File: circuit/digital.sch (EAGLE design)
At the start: 28 parts, among them IC1 MCP1701-5V, IC2 MCP1700-3.3V, X1 MINI-USB-SCHIELD-32005-301

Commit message: - вывели 4 IO пина на всяк случай, для LCD
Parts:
- added X10, X9: (no value), con-phoenix-254:MPT4
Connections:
- new net N$10: U$1G$9.PD5, X10-4.1
- new net N$6: U$1G$9.PD2, X10-1.1
- new net N$8: U$1G$9.PD3, X10-2.1
- new net N$9: U$1G$9.PD4, X10-3.1
- new net SWCLK: U$1G$2.PA14, X9-3.1
- new net SWDIO: U$1G$2.PA13, X9-2.1
- net +3V3: now also X9-1.1
- net GND: now also X9-4.1
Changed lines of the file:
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@@
 <part name="C10" library="rcl" deviceset="C-EU" device="C0603" value="1mk"/>
 <part name="P+2" library="supply1" deviceset="+5V" device=""/>
+<part name="X9" library="con-phoenix-254" deviceset="MPT4" device=""/>
+<part name="+3V4" library="supply1" deviceset="+3V3" device=""/>
+<part name="GND12" library="supply1" deviceset="GND" device=""/>
+<part name="X10" library="con-phoenix-254" deviceset="MPT4" device=""/>
 </parts>
 <sheets>
@@
 <instance part="C10" gate="G$1" x="25.4" y="93.98"/>
 <instance part="P+2" gate="1" x="25.4" y="104.14"/>
+<instance part="X9" gate="-1" x="177.8" y="5.08"/>
+<instance part="X9" gate="-2" x="177.8" y="0"/>
+<instance part="X9" gate="-3" x="177.8" y="-5.08"/>
+<instance part="X9" gate="-4" x="177.8" y="-10.16"/>
+<instance part="+3V4" gate="G$1" x="170.18" y="10.16"/>
+<instance part="GND12" gate="1" x="170.18" y="-15.24"/>
+<instance part="X10" gate="-1" x="127" y="-48.26"/>
+<instance part="X10" gate="-2" x="127" y="-53.34"/>
+<instance part="X10" gate="-3" x="127" y="-58.42"/>
+<instance part="X10" gate="-4" x="127" y="-63.5"/>
 </instances>
 <busses>
@@
 <junction x="12.7" y="88.9"/>
 <junction x="-2.54" y="88.9"/>
+</segment>
+<segment>
+<pinref part="GND12" gate="1" pin="GND"/>
+<wire x1="170.18" y1="-12.7" x2="170.18" y2="-10.16" width="0.1524" layer="91"/>
+<pinref part="X9" gate="-4" pin="1"/>
+<wire x1="170.18" y1="-10.16" x2="175.26" y2="-10.16" width="0.1524" layer="91"/>
 </segment>
 </net>
@@
 <junction x="0" y="40.64"/>
 </segment>
+<segment>
+<pinref part="X9" gate="-1" pin="1"/>
+<pinref part="+3V4" gate="G$1" pin="+3V3"/>
+<wire x1="175.26" y1="5.08" x2="170.18" y2="5.08" width="0.1524" layer="91"/>
+<wire x1="170.18" y1="5.08" x2="170.18" y2="7.62" width="0.1524" layer="91"/>
+</segment>
 </net>
 <net name="V+" class="0">
@@
 </segment>
 </net>
+<net name="SWDIO" class="0">
+<segment>
+<pinref part="U$1" gate="G$2" pin="PA13"/>
+<wire x1="50.8" y1="15.24" x2="40.64" y2="15.24" width="0.1524" layer="91"/>
+<label x="40.64" y="15.494" size="1.778" layer="95"/>
+</segment>
+<segment>
+<pinref part="X9" gate="-2" pin="1"/>
+<wire x1="175.26" y1="0" x2="162.56" y2="0" width="0.1524" layer="91"/>
+<label x="162.814" y="0.508" size="1.778" layer="95"/>
+</segment>
+</net>
+<net name="SWCLK" class="0">
+<segment>
+<pinref part="U$1" gate="G$2" pin="PA14"/>
+<wire x1="50.8" y1="12.7" x2="40.64" y2="12.7" width="0.1524" layer="91"/>
+<label x="40.386" y="12.954" size="1.778" layer="95"/>
+</segment>
+<segment>
+<pinref part="X9" gate="-3" pin="1"/>
+<wire x1="175.26" y1="-5.08" x2="162.56" y2="-5.08" width="0.1524" layer="91"/>
+<label x="162.814" y="-4.572" size="1.778" layer="95"/>
+</segment>
+</net>
+<net name="N$6" class="0">
+<segment>
+<pinref part="U$1" gate="G$9" pin="PD2"/>
+<wire x1="86.36" y1="-53.34" x2="114.3" y2="-53.34" width="0.1524" layer="91"/>
+<wire x1="114.3" y1="-53.34" x2="114.3" y2="-48.26" width="0.1524" layer="91"/>
+<pinref part="X10" gate="-1" pin="1"/>
+<wire x1="114.3" y1="-48.26" x2="124.46" y2="-48.26" width="0.1524" layer="91"/>
+</segment>
+</net>
+<net name="N$8" class="0">
+<segment>
+<pinref part="U$1" gate="G$9" pin="PD3"/>
+<wire x1="86.36" y1="-55.88" x2="119.38" y2="-55.88" width="0.1524" layer="91"/>
+<wire x1="119.38" y1="-55.88" x2="119.38" y2="-53.34" width="0.1524" layer="91"/>
+<pinref part="X10" gate="-2" pin="1"/>
+<wire x1="119.38" y1="-53.34" x2="124.46" y2="-53.34" width="0.1524" layer="91"/>
+</segment>
+</net>
+<net name="N$9" class="0">
+<segment>
+<pinref part="U$1" gate="G$9" pin="PD4"/>
+<pinref part="X10" gate="-3" pin="1"/>
+<wire x1="86.36" y1="-58.42" x2="124.46" y2="-58.42" width="0.1524" layer="91"/>
+</segment>
+</net>
+<net name="N$10" class="0">
+<segment>
+<pinref part="U$1" gate="G$9" pin="PD5"/>
+<wire x1="86.36" y1="-60.96" x2="121.92" y2="-60.96" width="0.1524" layer="91"/>
+<wire x1="121.92" y1="-60.96" x2="121.92" y2="-63.5" width="0.1524" layer="91"/>
+<pinref part="X10" gate="-4" pin="1"/>
+<wire x1="121.92" y1="-63.5" x2="124.46" y2="-63.5" width="0.1524" layer="91"/>
+</segment>
+</net>

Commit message: - подтяжка по USB
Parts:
- added R4: 1.5k, rcl:R-EU_R0603
- L2: value MMZ1608B102C -> 100mk
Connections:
- net +3V3: now also R4.1
- net GND: now also U$1G$11.VBAT
- net N$2: now also R4.2
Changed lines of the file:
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@@
 </classes>
 <parts>
-<part name="L2" library="rcl" deviceset="L-US" device="0204/7" value="MMZ1608B102C"/>
+<part name="L2" library="rcl" deviceset="L-US" device="0204/7" value="100mk"/>
 <part name="C11" library="rcl" deviceset="C-EU" device="C0603" value="100n"/>
 <part name="C12" library="rcl" deviceset="C-EU" device="C0805" value="10mk"/>
@@
 <part name="GND12" library="supply1" deviceset="GND" device=""/>
 <part name="X10" library="con-phoenix-254" deviceset="MPT4" device=""/>
+<part name="R4" library="rcl" deviceset="R-EU_" device="R0603" value="1.5k"/>
+<part name="+3V5" library="supply1" deviceset="+3V3" device=""/>
 </parts>
 <sheets>
@@
 <instance part="X10" gate="-3" x="127" y="-58.42"/>
 <instance part="X10" gate="-4" x="127" y="-63.5"/>
+<instance part="R4" gate="G$1" x="45.72" y="48.26" rot="R90"/>
+<instance part="+3V5" gate="G$1" x="40.64" y="45.72"/>
 </instances>
 <busses>
@@
 <pinref part="X1" gate="G$1" pin="3"/>
 <pinref part="R2" gate="G$1" pin="2"/>
-<wire x1="53.34" y1="53.34" x2="43.18" y2="53.34" width="0.1524" layer="91"/>
+<wire x1="53.34" y1="53.34" x2="45.72" y2="53.34" width="0.1524" layer="91"/>
+<wire x1="45.72" y1="53.34" x2="43.18" y2="53.34" width="0.1524" layer="91"/>
 <wire x1="43.18" y1="53.34" x2="43.18" y2="50.8" width="0.1524" layer="91"/>
+<pinref part="R4" gate="G$1" pin="2"/>
+<junction x="45.72" y="53.34"/>
 </segment>
 </net>
@@
 <junction x="-7.62" y="25.4"/>
 <junction x="-7.62" y="33.02"/>
+<pinref part="U$1" gate="G$11" pin="VBAT"/>
+<wire x1="12.7" y1="2.54" x2="12.7" y2="7.62" width="0.1524" layer="91"/>
 </segment>
 <segment>
@@
 <wire x1="170.18" y1="5.08" x2="170.18" y2="7.62" width="0.1524" layer="91"/>
 </segment>
-</net>
+<segment>
+<pinref part="R4" gate="G$1" pin="1"/>
+<pinref part="+3V5" gate="G$1" pin="+3V3"/>
+<wire x1="45.72" y1="43.18" x2="40.64" y2="43.18" width="0.1524" layer="91"/>
+</segment>
+</net>

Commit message: - косметические изменения
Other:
- note added: "ADC3_IN1"
- note added: "ADC4_IN1"
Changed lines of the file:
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@@
 <sheet>
 <plain>
+<text x="-10.16" y="-38.1" size="1.778" layer="91">ADC4_IN1</text>
+<text x="99.06" y="0" size="1.778" layer="91">ADC3_IN1</text>
 </plain>
 <instances>

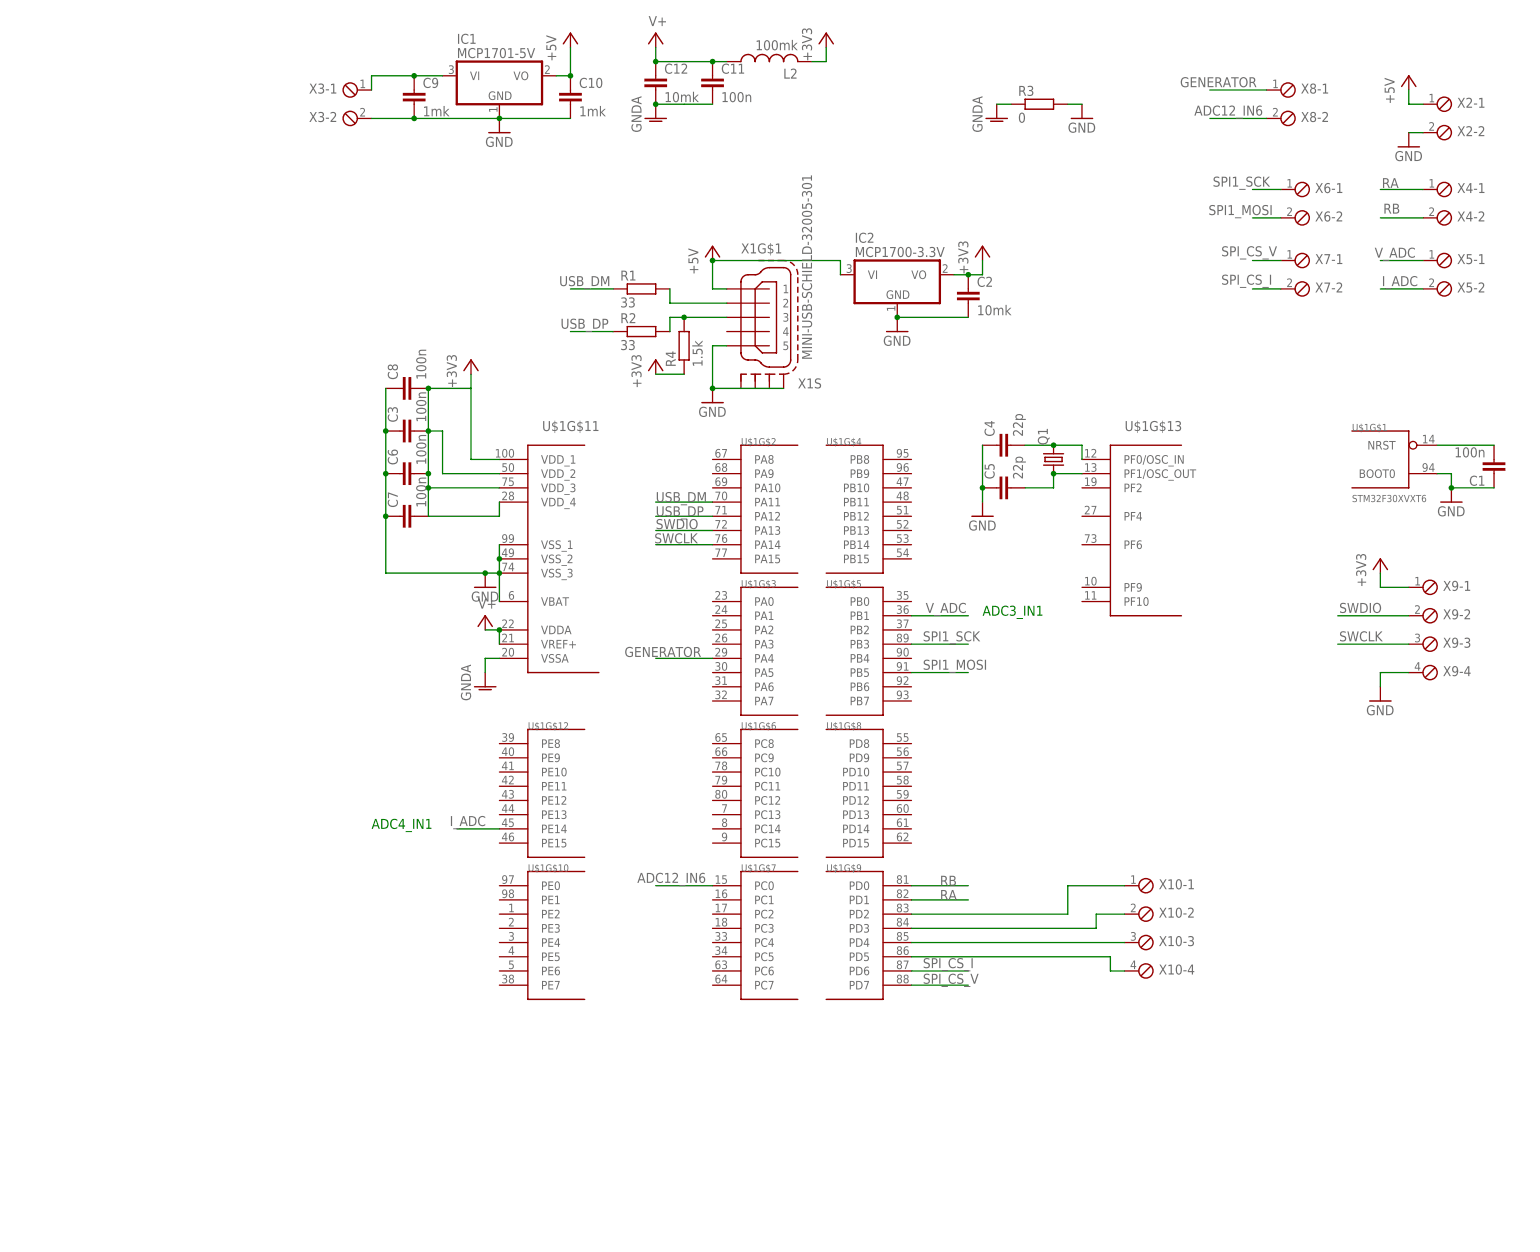
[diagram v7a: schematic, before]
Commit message: - на цифровой схеме добавили разъем для Nokia 5110, коннекторы для переключения питания, объединили восточный разъем - на аналоговой схеме добавили включение 3.3 nF конденсатор, для фильтрации высокочастотных шумов ADC
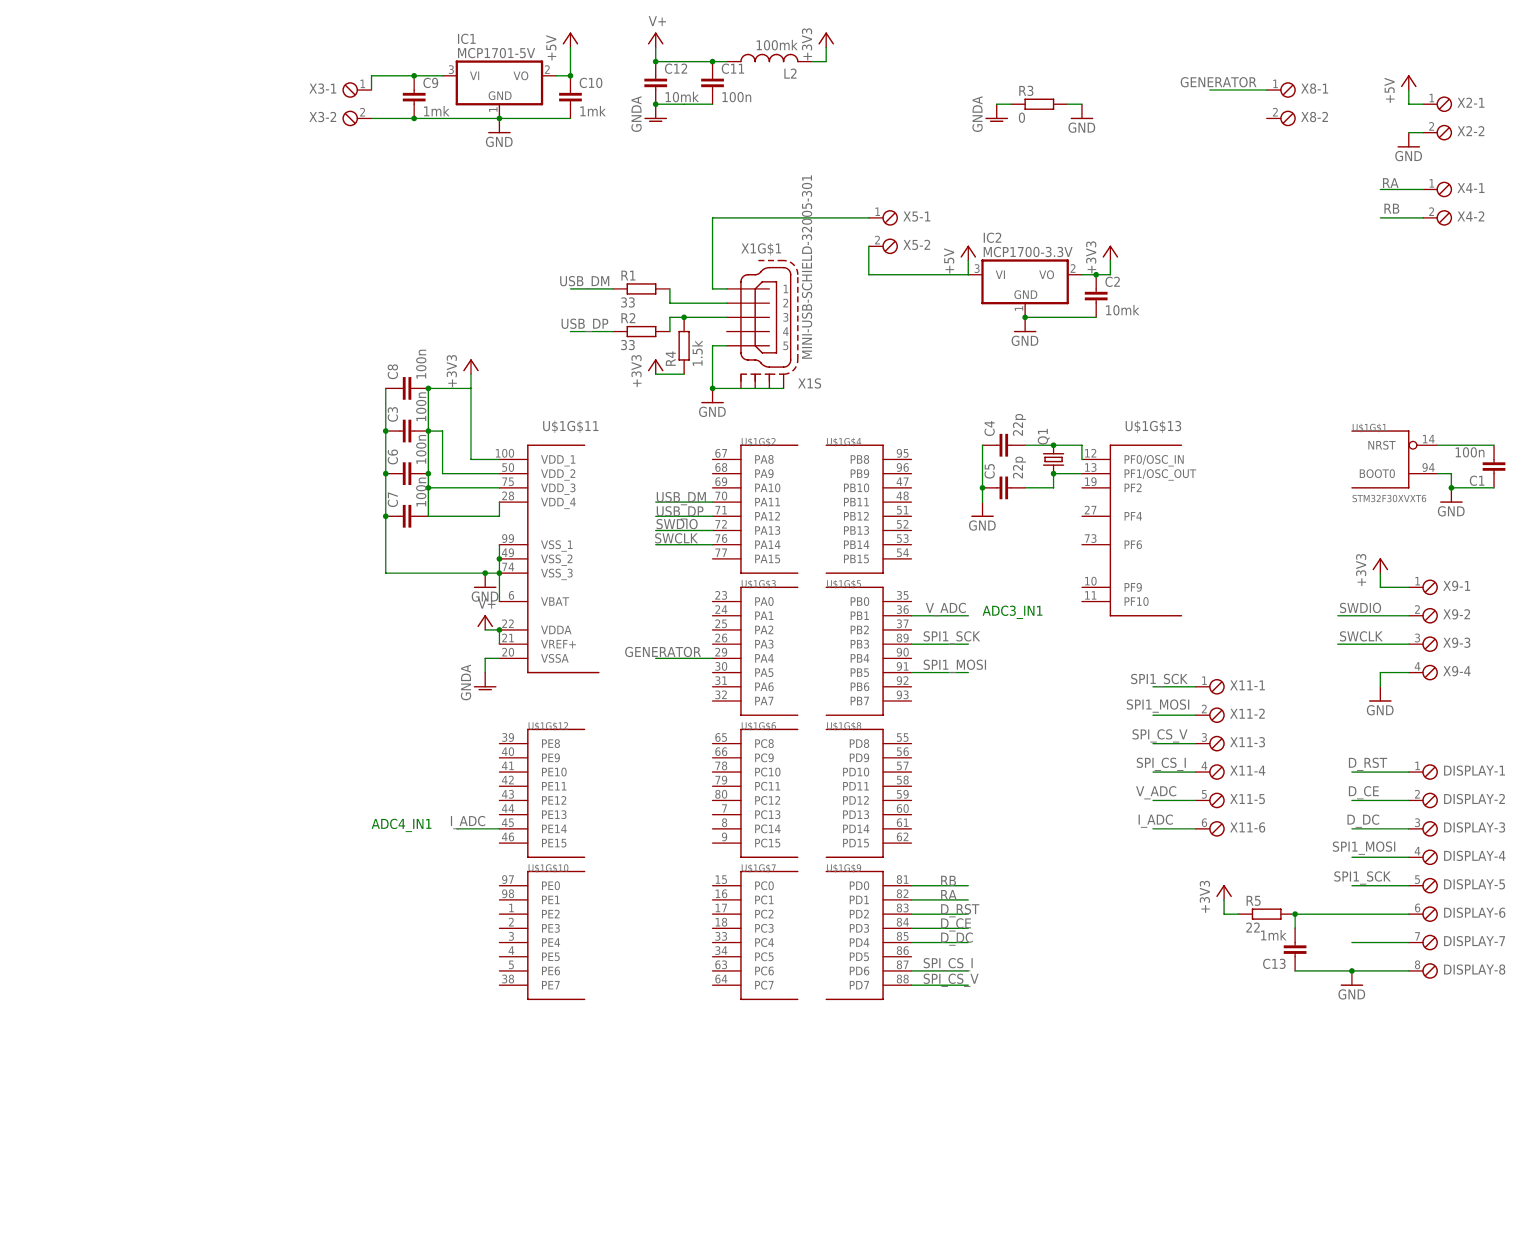
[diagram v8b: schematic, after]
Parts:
- removed X10: (no value), con-phoenix-254:MPT4
- removed X6, X7: (no value), con-phoenix-254:MPT2
- added C13: 1mk, rcl:C-EUC0603
- added DISPLAY: (no value), con-phoenix-254:MPT8
- added R5: 22, rcl:R-EU_R0603
- added X11: (no value), con-phoenix-254:MPT6
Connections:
- removed net ADC12_IN6: U$1G$7.PC0, X8-2.1
- removed net N$10: U$1G$9.PD5, X10-4.1
- removed net N$9: U$1G$9.PD4, X10-3.1
- new net D_CE: DISPLAY-2.1, U$1G$9.PD3
- new net D_DC: DISPLAY-3.1, U$1G$9.PD4
- new net D_RST: DISPLAY-1.1, U$1G$9.PD2
- new net N$13: DISPLAY-7.1
- net +3V3: now also R5.1
- net +5V: now also X5-2.1; no longer X1G$1.1
- net GND: now also C13.1, DISPLAY-8.1
- net I_ADC: now also X11-6.1; no longer X5-2.1
- net N$6: now also C13.2, DISPLAY-6.1, R5.2; no longer U$1G$9.PD2, X10-1.1
- net N$8: now also X1G$1.1, X5-1.1; no longer U$1G$9.PD3, X10-2.1
- net SPI1_MOSI: now also DISPLAY-4.1, X11-2.1; no longer X6-2.1
- net SPI1_SCK: now also DISPLAY-5.1, X11-1.1; no longer X6-1.1
- net SPI_CS_I: now also X11-4.1; no longer X7-2.1
- net SPI_CS_V: now also X11-3.1; no longer X7-1.1
- net V_ADC: now also X11-5.1; no longer X5-1.1
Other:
- moved on the sheet: C2, IC2, X5-1, X5-2
